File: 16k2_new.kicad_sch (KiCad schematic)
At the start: 21 parts, among them J1 Conn_01x02_Socket, J2 XIAO esp32c3 right, J3 XIAO esp32c3 right, U1 CD74HC4067M, U3 XIAO-ESP32-C3-SMD

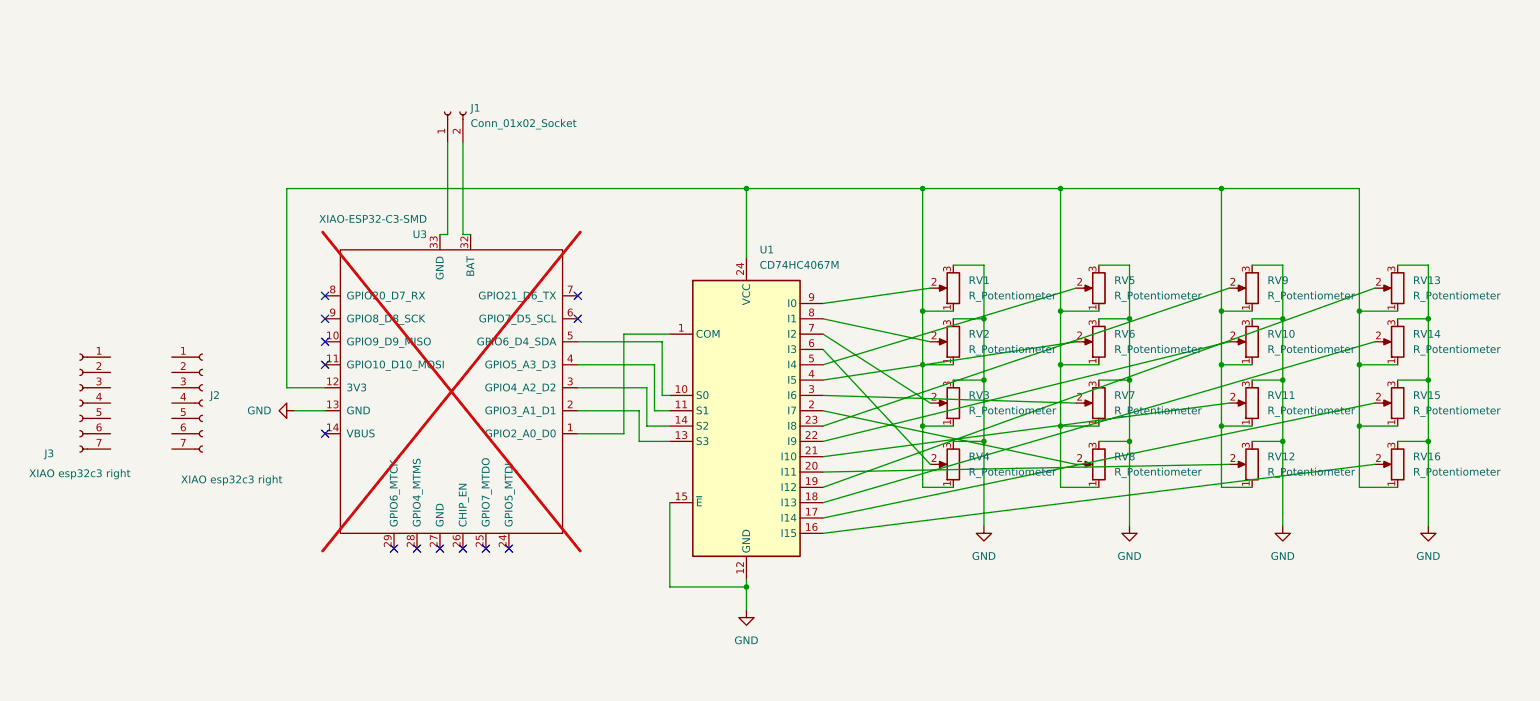
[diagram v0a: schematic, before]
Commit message: Correct mistakenly removed file from backups
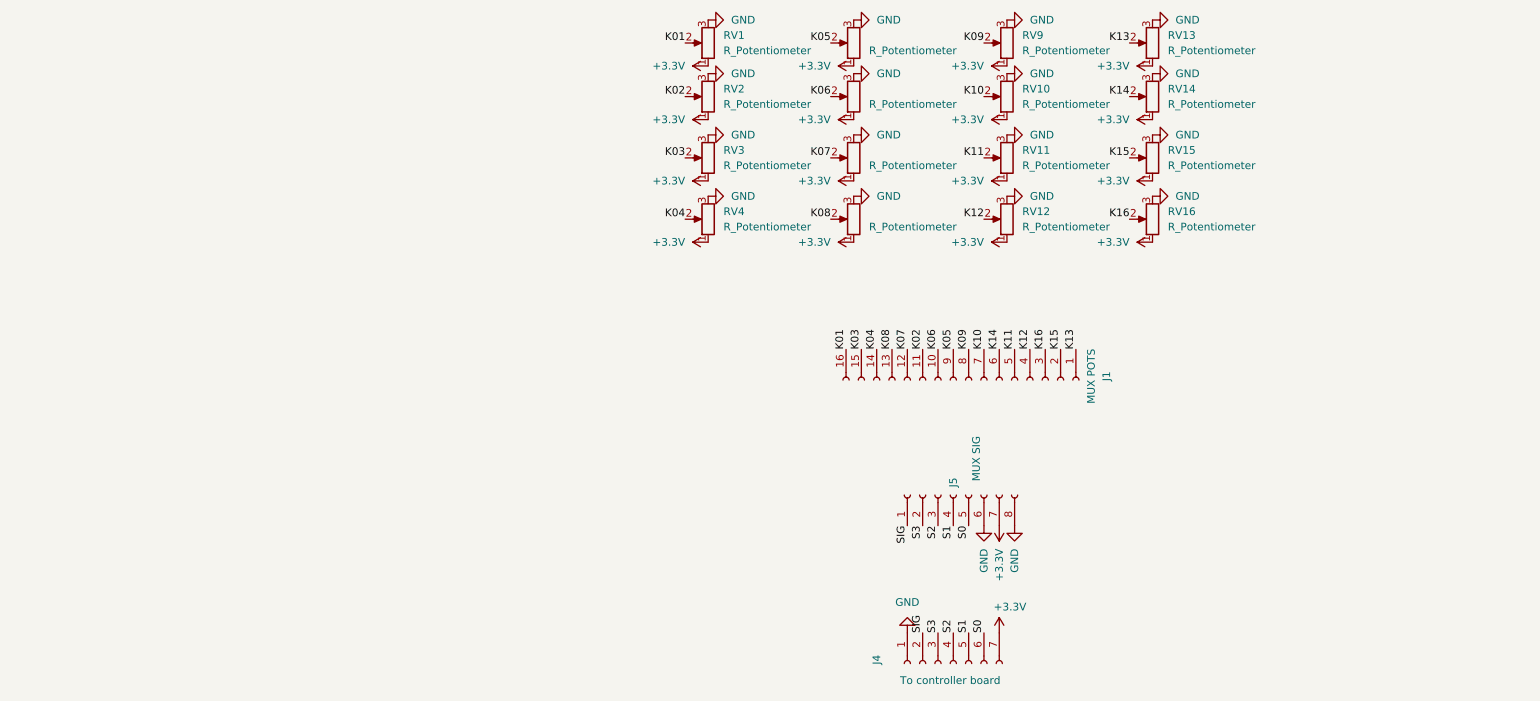
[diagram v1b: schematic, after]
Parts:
- removed J1: Conn_01x02_Socket, symbol Connector:Conn_01x02_Socket
- removed J2, J3: XIAO esp32c3 right, symbol Connector:Conn_01x07_Socket
- removed U1: CD74HC4067M, Package_SO:SOIC-24W_7.5x15.4mm_P1.27mm, symbol 74xx:CD74HC4067M
- removed U3: XIAO-ESP32-C3-SMD, Seeed_Studio_XIAO_Series:XIAO-ESP32-C3-SMD, symbol User libs:XIAO-ESP32-C3-SMD
- added J1: MUX POTS, Connector_PinSocket_2.54mm:PinSocket_1x16_P2.54mm_Vertical, symbol Connector:Conn_01x16_Socket
- added J4: To controller board, Connector_JST:JST_XH_B7B-XH-AM_1x07_P2.50mm_Vertical, symbol Connector:Conn_01x07_Socket
- added J5: MUX SIG, Connector_PinSocket_2.54mm:PinSocket_1x08_P2.54mm_Vertical, symbol Connector:Conn_01x08_Socket
- RV1, RV10, RV11, RV12, RV13, RV14, RV15, RV16, RV2, RV3, RV4, RV5, RV6, RV7, RV8, RV9: footprint Potentiometer_THT:Potentiometer_Alps_RK09K_Single_Vertical -> Custom:Potentiometer_Alps_RK09K_Single_Vertical
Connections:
- net GND: now also J4.1 (Pin_1), J5.6 (Pin_6), J5.8 (Pin_8)
- net +3.3V: now reaches RV1.1, RV10.1, RV11.1, RV12.1, RV13.1, RV14.1, RV15.1, RV16.1, RV2.1, RV3.1, RV4.1, RV5.1, RV6.1, RV7.1, RV8.1, RV9.1
- net +3.3V: now also J4.7 (Pin_7), J5.7 (Pin_7)
- net K14: now reaches RV14.2
- net K14: now also J1.6 (Pin_6)
- net K02: now reaches RV2.2
- net K02: now also J1.11 (Pin_11)
- net K08: now reaches RV8.2
- net K08: now also J1.13 (Pin_13)
- net K07: now reaches RV7.2
- net K07: now also J1.12 (Pin_12)
- net K16: now reaches RV16.2
- net K16: now also J1.3 (Pin_3)
- net K15: now reaches RV15.2
- net K15: now also J1.2 (Pin_2)
- net K13: now reaches RV13.2
- net K13: now also J1.1 (Pin_1)
- net K12: now reaches RV12.2
- net K12: now also J1.4 (Pin_4)
- net K11: now reaches RV11.2
- net K11: now also J1.5 (Pin_5)
- net K10: now reaches RV10.2
- net K10: now also J1.7 (Pin_7)
- net K09: now reaches RV9.2
- net K09: now also J1.8 (Pin_8)
- net K06: now reaches RV6.2
- net K06: now also J1.10 (Pin_10)
- net K05: now reaches RV5.2
- net K05: now also J1.9 (Pin_9)
- net K04: now reaches RV4.2
- net K04: now also J1.14 (Pin_14)
- net K03: now reaches RV3.2
- net K03: now also J1.15 (Pin_15)
- net K01: now reaches RV1.2
- net K01: now also J1.16 (Pin_16)
- new net S0: J4.6 (Pin_6), J5.5 (Pin_5)
- new net S1: J4.5 (Pin_5), J5.4 (Pin_4)
- new net S2: J4.4 (Pin_4), J5.3 (Pin_3)
- new net S3: J4.3 (Pin_3), J5.2 (Pin_2)
- new net SIG: J4.2 (Pin_2), J5.1 (Pin_1)
- no-connect marks 13 -> 0
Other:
- moved on the sheet: RV1, RV10, RV11, RV12, RV13, RV14, RV15, RV16, RV2, RV3, RV4, RV9
